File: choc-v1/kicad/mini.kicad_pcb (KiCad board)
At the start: 2 copper layers, 126.3 x 89.3 mm, 40 parts

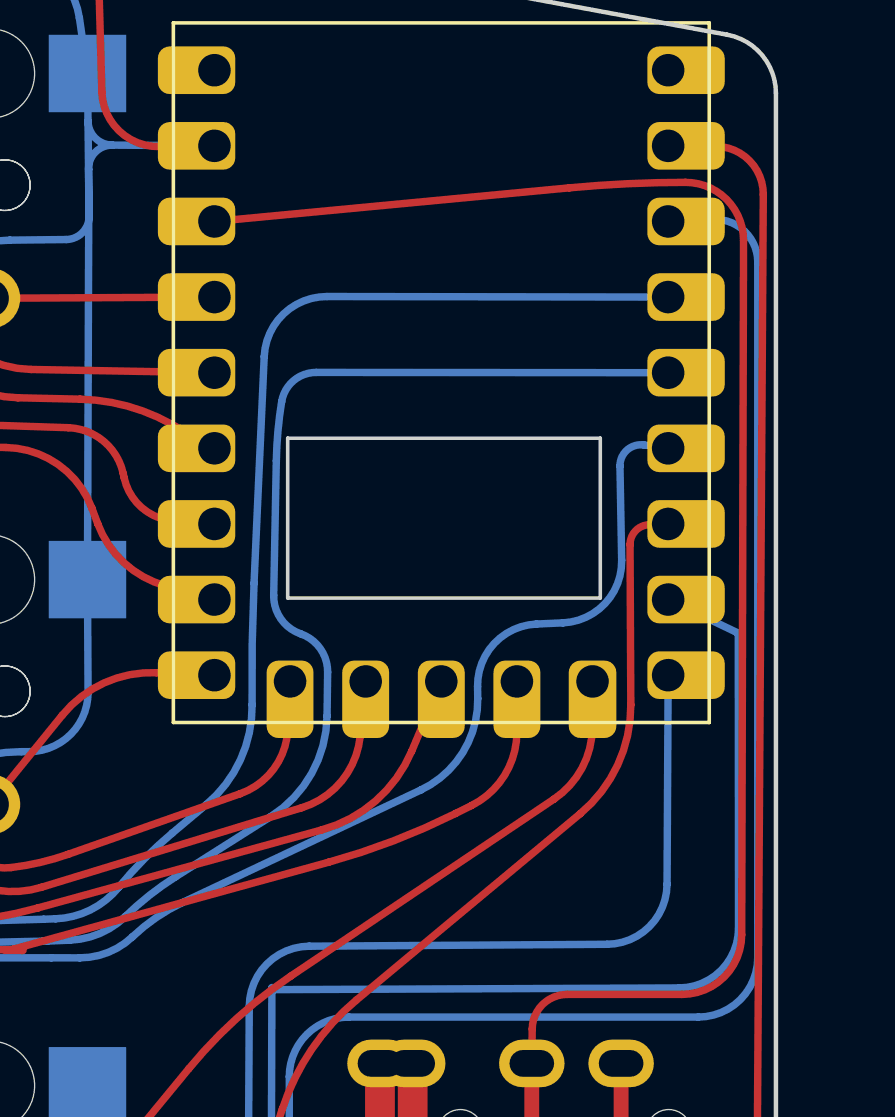
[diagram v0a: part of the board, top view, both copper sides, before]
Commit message: add more clearance to 3.3v route
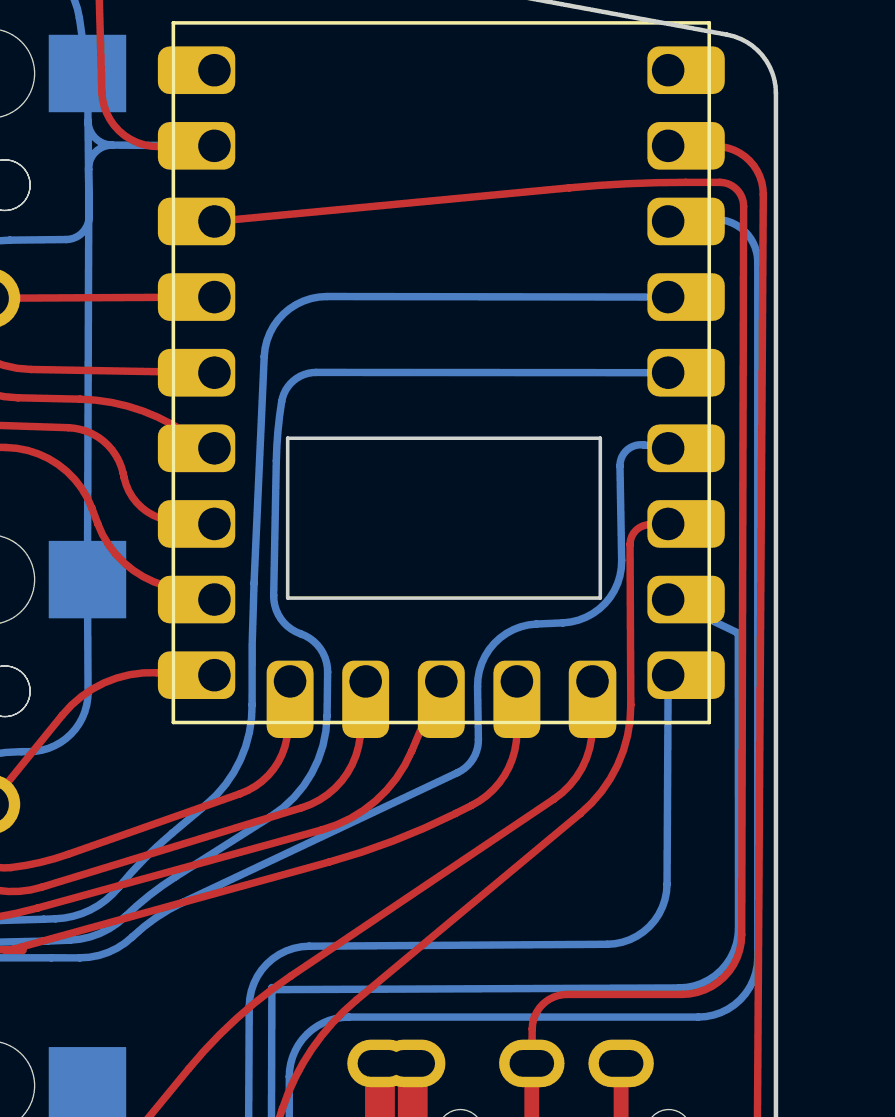
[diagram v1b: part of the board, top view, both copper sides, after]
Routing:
- net P3V3: track 56.7 -> 57.2 mm
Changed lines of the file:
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@@
   (segment (start 175.847939 79.883836) (end 170.989335 79.878564) (width 0.25) (layer "B.Cu") (net 8))
   (segment (start 132.717751 79.790275) (end 130.686041 84.870163) (width 0.25) (layer "B.Cu") (net 8))
-  (segment (start 192.215566 74.251548) (end 184.208716 78.031928) (width 0.25) (layer "B.Cu") (net 8))
-  (segment (start 194.124736 70.776895) (end 194.131065 71.1751) (width 0.25) (layer "B.Cu") (net 8))
+  (segment (start 193.458135 73.664877) (end 184.208716 78.031928) (width 0.25) (layer "B.Cu") (net 8))
+  (segment (start 194.124736 70.776895) (end 194.152902 72.549023) (width 0.25) (layer "B.Cu") (net 8))
   (segment (start 144.671582 82.365614) (end 145.876301 79.492432) (width 0.25) (layer "B.Cu") (net 8))
   (segment (start 196.102516 68.676097) (end 196.992728 68.636532) (width 0.25) (layer "B.Cu") (net 8))
@@
   (arc (start 144.671582 82.365614) (mid 143.742935 83.533897) (end 142.341021 84.045669) (width 0.25) (layer "B.Cu") (net 8))
   (arc (start 166.384858 79.326958) (mid 168.670785 79.738918) (end 170.989335 79.878564) (width 0.25) (layer "B.Cu") (net 8))
-  (arc (start 194.131065 71.1751) (mid 193.626305 72.99537) (end 192.215566 74.251548) (width 0.25) (layer "B.Cu") (net 8))
+  (arc (start 194.152902 72.549023) (mid 193.969822 73.209251) (end 193.458135 73.664877) (width 0.25) (layer "B.Cu") (net 8))
   (arc (start 199.709514 62.660701) (mid 199.144594 62.83182) (end 198.907449 63.372354) (width 0.25) (layer "B.Cu") (net 8))
   (segment (start 136.497219 59.164007) (end 137.274411 57.594137) (width 0.25) (layer "F.Cu") (net 9))
@@
   (arc (start 189.800024 81.878003) (mid 188.385811 82.463788) (end 187.800026 83.878001) (width 0.25) (layer "B.Cu") (net 19))
   (arc (start 187.800026 101.511675) (mid 188.234219 103.561648) (end 189.462232 105.259559) (width 0.25) (layer "B.Cu") (net 19))
+  (segment (start 201.110248 53.840316) (end 202.257993 53.840344) (width 0.25) (layer "F.Cu") (net 20))
   (segment (start 195.959952 82.27519) (end 195.946574 83.433756) (width 0.25) (layer "F.Cu") (net 20))
   (segment (start 195.946574 83.433756) (end 195.946574 88.033756) (width 0.5) (layer "F.Cu") (net 20))
   (segment (start 197.131973 81.116625) (end 200.990277 81.116625) (width 0.25) (layer "F.Cu") (net 20))
-  (segment (start 203.058542 55.793784) (end 202.996681 79.115535) (width 0.25) (layer "F.Cu") (net 20))
+  (segment (start 203.061586 54.646091) (end 202.996681 79.115535) (width 0.25) (layer "F.Cu") (net 20))
   (segment (start 197.211997 54.024476) (end 185.286574 55.153756) (width 0.25) (layer "F.Cu") (net 20))
   (arc (start 201.110248 53.840316) (mid 199.158948 53.886381) (end 197.211997 54.024476) (width 0.25) (layer "F.Cu") (net 20))
-  (arc (start 203.058542 55.793784) (mid 202.48973 54.412788) (end 201.110248 53.840316) (width 0.25) (layer "F.Cu") (net 20))
+  (arc (start 203.061586 54.646091) (mid 202.826975 54.076479) (end 202.257993 53.840344) (width 0.25) (layer "F.Cu") (net 20))
   (arc (start 197.131973 81.116625) (mid 196.307972 81.455153) (end 195.959952 82.27519) (width 0.25) (layer "F.Cu") (net 20))
   (arc (start 202.996681 79.115535) (mid 202.407141 80.53084) (end 200.990277 81.116625) (width 0.25) (layer "F.Cu") (net 20))
